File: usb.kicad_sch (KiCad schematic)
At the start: 17 parts, among them J3 USB_C_Receptacle_USB2.0_14P, J4 USB_C_Receptacle_USB2.0_14P, J5 USB_C_Receptacle_USB2.0_14P, J6 CONN_02X03, U1 ECP5U_12_CABGA256, U5 USBLC6-2P6, U6 USBLC6-2P6, U7 FT231XQ, U8 USBLC6-2P6

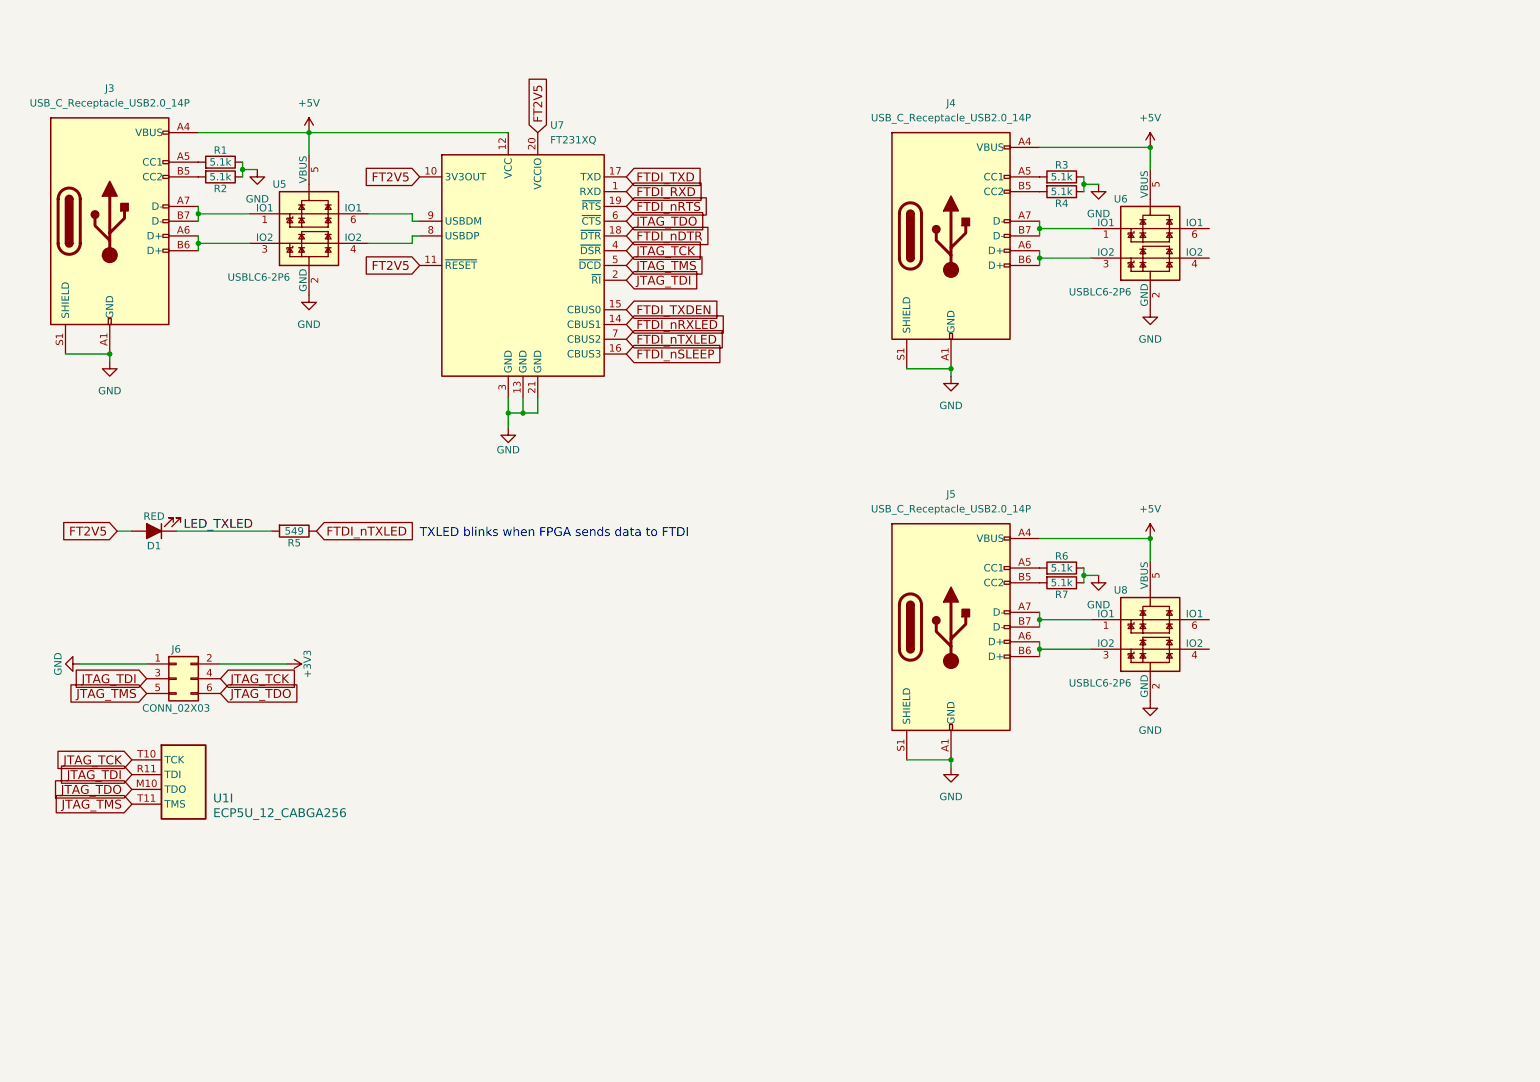
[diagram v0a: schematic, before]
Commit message: Routed HDMI, usb, rotated chip and more
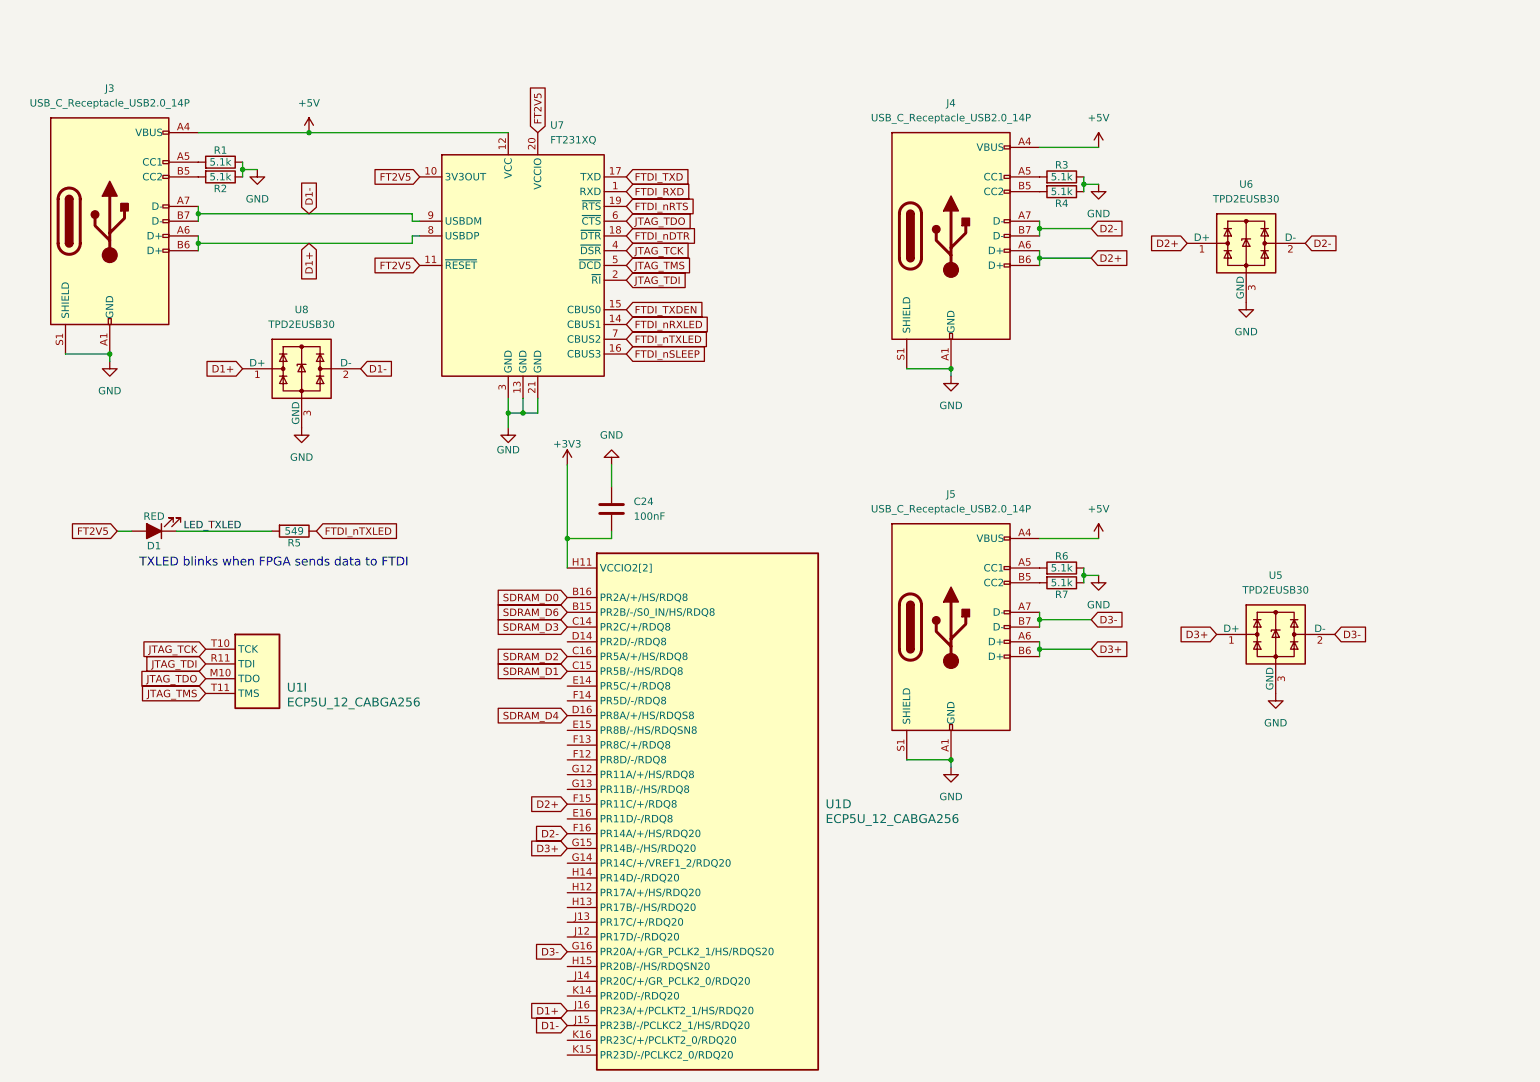
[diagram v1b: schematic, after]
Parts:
- removed J6: CONN_02X03, Connector_PinHeader_2.54mm:PinHeader_2x03_P2.54mm_Vertical, symbol Connector_Generic:Conn_02x03_Odd_Even
- removed U5, U6, U8: USBLC6-2P6, Package_TO_SOT_SMD:SOT-666, symbol josh-ic:USBLC6-2SC6
- added C24: 100nF, Capacitor_SMD:C_0402_1005Metric, symbol Device:C
- added unit 4 of U1
- added U5, U6, U8: TPD2EUSB30, Package_TO_SOT_SMD:Texas_DRT-3, symbol Power_Protection:TPD2EUSB30
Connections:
- net +3V3: now also C24.2, U1.H11 (VCCIO2[2]), U1.J11 (VCCIO2[2])
- net GND: now also C24.1, U5.3 (GND), U6.3 (GND), U8.3 (GND)
- net D1+: now reaches U7.8 (USBDP)
- net D1+: now also J3.A6 (D+), J3.B6 (D+), U1.J16 (PR23A/+/PCLKT2_1/HS/RDQ20), U8.1 (D+)
- net D1-: now reaches U7.9 (USBDM)
- net D1-: now also J3.A7 (D-), J3.B7 (D-), U1.J15 (PR23B/-/PCLKC2_1/HS/RDQ20), U8.2 (D-)
- net D3-: now reaches J5.A7 (D-), J5.B7 (D-)
- net D3-: now also U1.G16 (PR20A/+/GR_PCLK2_1/HS/RDQS20), U5.2 (D-)
- net D3+: now reaches J5.A6 (D+), J5.B6 (D+)
- net D3+: now also U1.G15 (PR14B/-/HS/RDQ20), U5.1 (D+)
- net D2-: now reaches J4.A7 (D-), J4.B7 (D-)
- net D2-: now also U1.F16 (PR14A/+/HS/RDQ20), U6.2 (D-)
- net D2+: now reaches J4.A6 (D+), J4.B6 (D+)
- net D2+: now also U1.F15 (PR11C/+/RDQ8), U6.1 (D+)
- new net SDRAM_D0: U1.B16 (PR2A/+/HS/RDQ8)
- new net SDRAM_D1: U1.C15 (PR5B/-/HS/RDQ8)
- new net SDRAM_D2: U1.C16 (PR5A/+/HS/RDQ8)
- new net SDRAM_D3: U1.C14 (PR2C/+/RDQ8)
- new net SDRAM_D4: U1.D16 (PR8A/+/HS/RDQS8)
- new net SDRAM_D6: U1.B15 (PR2B/-/S0_IN/HS/RDQ8)
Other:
- moved on the sheet: U1I

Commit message: Stash
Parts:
- removed C24: 100nF, Capacitor_SMD:C_0402_1005Metric, symbol Device:C
- D1: footprint LED_SMD:LED_0805_2012Metric -> LED_SMD:LED_0603_1608Metric
- J3, J4, J5: footprint Connector_USB:USB_C_Receptacle_Palconn_UTC16-G -> Connector_USB:USB_C_Receptacle_GCT_USB4105-xx-A_16P_TopMnt_Horizontal
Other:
- moved on the sheet: D1, J3, J4, J5, R1, R2, R3, R4, R5, R6, R7, U1D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

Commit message: Rev 1
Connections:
- net D2+: now also U1.F16 (PR14A/+/HS/RDQ20); no longer U1.F15 (PR11C/+/RDQ8)
- net D2-: now also U1.G15 (PR14B/-/HS/RDQ20); no longer U1.F16 (PR14A/+/HS/RDQ20)
- net D3+: now also U1.H15 (PR20B/-/HS/RDQSN20); no longer U1.G15 (PR14B/-/HS/RDQ20)
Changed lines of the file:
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@@
 	(global_label "D2+"
 		(shape input)
-		(at 213.36 81.28 180)
-		(fields_autoplaced yes)
-		(effects
-			(font
-				(size 1.27 1.27)
-			)
-			(justify right)
-		)
-		(property "Intersheetrefs" "${INTERSHEET_REFS}"
-			(at 206.3229 81.28 0)
+		(at 213.36 86.36 180)
+		(fields_autoplaced yes)
+		(effects
+			(font
+				(size 1.27 1.27)
+			)
+			(justify right)
+		)
+		(property "Intersheetrefs" "${INTERSHEET_REFS}"
+			(at 206.3229 86.36 0)
 			(effects
 				(font
@@
 	(global_label "D2-"
 		(shape input)
-		(at 213.36 86.36 180)
-		(fields_autoplaced yes)
-		(effects
-			(font
-				(size 1.27 1.27)
-			)
-			(justify right)
-		)
-		(property "Intersheetrefs" "${INTERSHEET_REFS}"
-			(at 206.3229 86.36 0)
+		(at 213.36 88.9 180)
+		(fields_autoplaced yes)
+		(effects
+			(font
+				(size 1.27 1.27)
+			)
+			(justify right)
+		)
+		(property "Intersheetrefs" "${INTERSHEET_REFS}"
+			(at 206.3229 88.9 0)
 			(effects
 				(font
@@
 	(global_label "D3+"
 		(shape input)
-		(at 213.36 88.9 180)
-		(fields_autoplaced yes)
-		(effects
-			(font
-				(size 1.27 1.27)
-			)
-			(justify right)
-		)
-		(property "Intersheetrefs" "${INTERSHEET_REFS}"
-			(at 206.3229 88.9 0)
-			(effects
-				(font
+		(at 213.36 109.22 180)
+		(fields_autoplaced yes)
+		(effects
+			(font
+				(size 1.27 1.27)
+			)
+			(justify right)
+		)
+		(property "Intersheetrefs" "${INTERSHEET_REFS}"
+			(at 206.3229 109.22 0)
+			(effects
+				(font
